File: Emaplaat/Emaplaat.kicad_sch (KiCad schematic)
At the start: 15 parts, among them IC1 ESP32-S3-WROOM-2-N32R16V, IC2 74HC595PW-Q100,118, IC3 74HC595PW-Q100,118

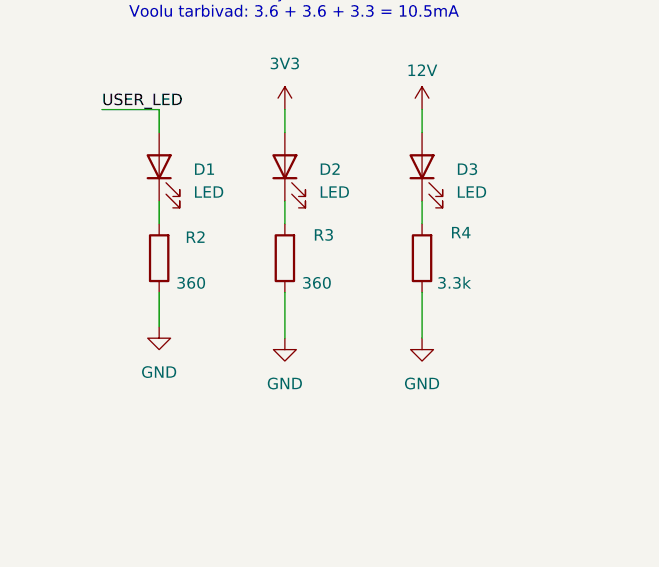
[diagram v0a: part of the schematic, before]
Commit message: ühe takisti muudatus
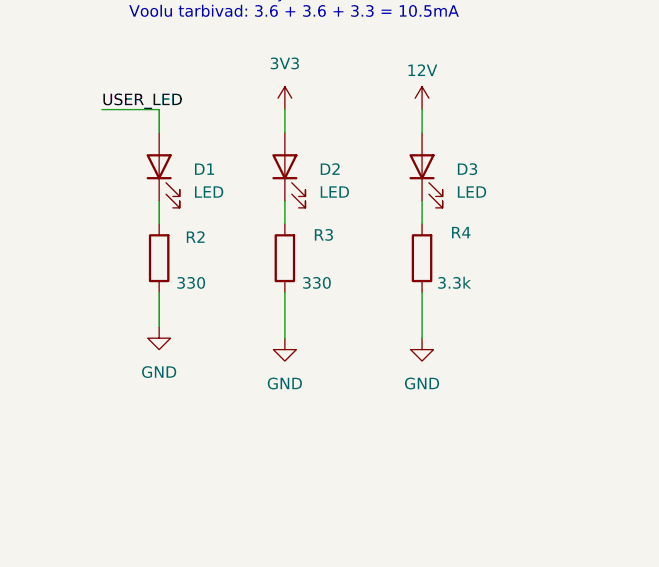
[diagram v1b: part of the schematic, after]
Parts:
- R2, R3: value 360 -> 330
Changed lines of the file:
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@@
 			)
 		)
-		(property "Value" "360"
+		(property "Value" "330"
 			(at 55.626 159.004 0)
 			(effects
@@
 			)
 		)
-		(property "Value" "360"
+		(property "Value" "330"
 			(at 41.656 159.004 0)
 			(effects

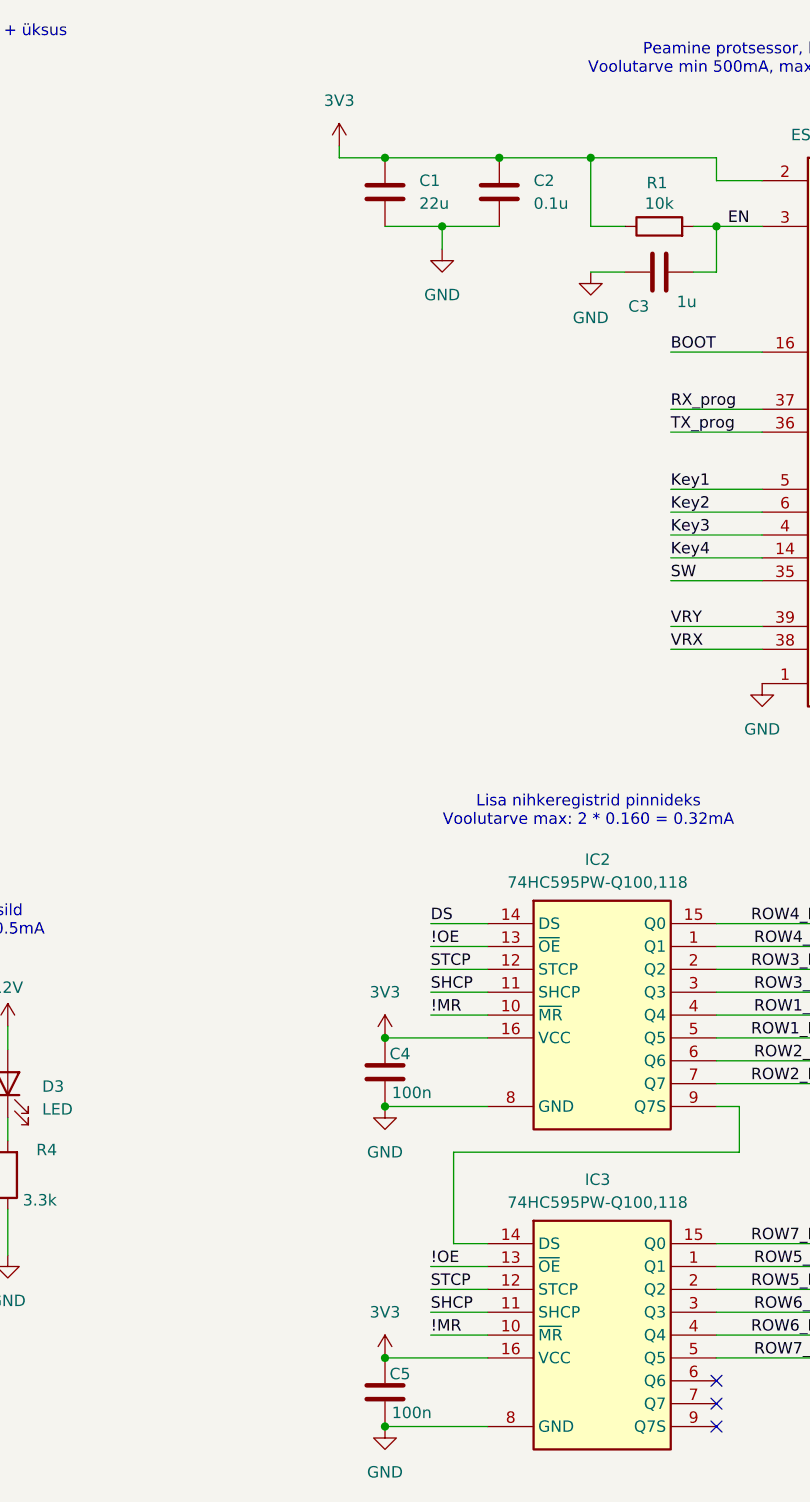
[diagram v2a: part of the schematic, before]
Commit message: Lisasin kondensaatorid, mis on >3.3u footprindi ja sümbolid. Sammuti liigutasin ESP32 ja USC-C ühendused plaadi äärtele
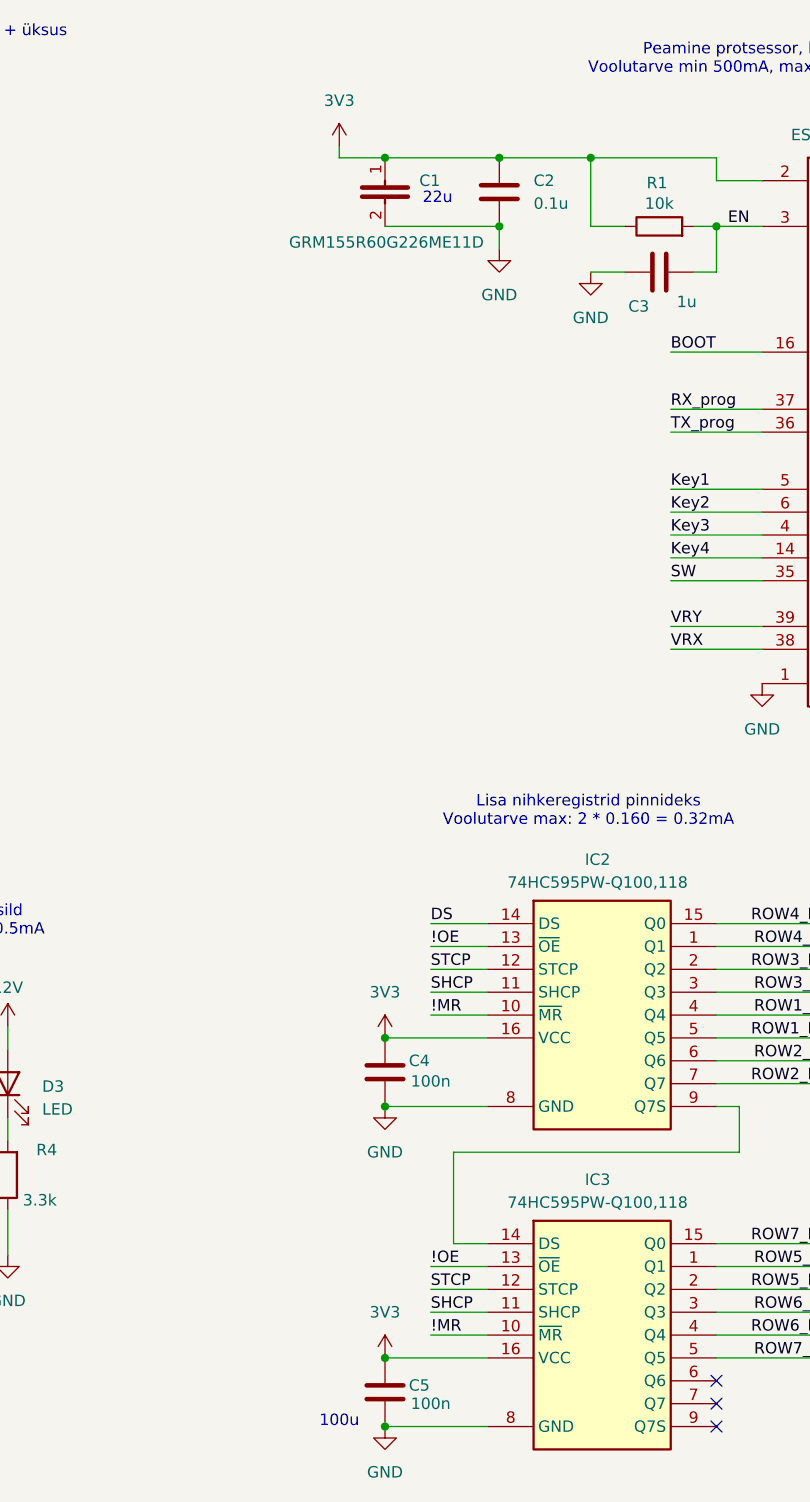
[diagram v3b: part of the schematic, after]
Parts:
- removed C1: 22u, Capacitor_SMD:C_0603_1608Metric_Pad1.08x0.95mm_HandSolder, symbol Device:C
- added C1: GRM155R60G226ME11D, CAPC1005X70N, symbol GRM155R60G226ME11D:GRM155R60G226ME11D
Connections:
- net 3V3: now also C4.2, C5.2, C1.1; no longer C4.1, C5.1
- net GND: now also C4.1, C5.1, C1.2; no longer C4.2, C5.2
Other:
- note added: "100u"
- note added: "22u"

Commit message: v1.2 bootstrapping pin parandus
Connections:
- net BOOT: now also IC1.27 (IO0); no longer IC1.16 (IO46)
- net COLUMN4: now also IC1.16 (IO46); no longer IC1.27 (IO0)
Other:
- note added: "IO0, IO3, IO45, IO46 on bootstrapping pinnid IO0 on vaja ainult kontollida bootmode'i jaoks"
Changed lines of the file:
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@@
+		)
+	)
+	(text "IO0, IO3, IO45, IO46 on bootstrapping pinnid\nIO0 on vaja ainult kontollida bootmode'i jaoks"
+		(exclude_from_sim no)
+		(at 116.332 67.31 0)
+		(effects
+			(font
+				(size 1.27 1.27)
+			)
 		)
 	)

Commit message: v1.3 pooleli
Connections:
- net !MR: now also IC1.12 (IO8); no longer IC1.13 (IO19)
- net !OE: now also IC1.11 (IO18); no longer IC1.10 (IO17)
- net COLUMN1: now also IC1.32 (IO39); no longer IC1.33 (IO40)
- net COLUMN10: now also IC1.19 (IO11); no longer IC1.21 (IO13)
- net COLUMN11: now also IC1.18 (IO10); no longer IC1.20 (IO12)
- net COLUMN12: now also IC1.17 (IO9); no longer IC1.19 (IO11)
- net COLUMN13: now also IC1.16 (IO46); no longer IC1.18 (IO10)
- net COLUMN14: now also IC1.15 (IO3); no longer IC1.17 (IO9)
- net COLUMN2: now also IC1.31 (IO38); no longer IC1.32 (IO39)
- net COLUMN3: now also IC1.26 (IO45); no longer IC1.31 (IO38)
- net COLUMN4: now also IC1.25 (IO48); no longer IC1.16 (IO46)
- net COLUMN5: now also IC1.24 (IO47); no longer IC1.26 (IO45)
- net COLUMN6: now also IC1.23 (IO21); no longer IC1.25 (IO48)
- net COLUMN7: now also IC1.22 (IO14); no longer IC1.24 (IO47)
- net COLUMN8: now also IC1.21 (IO13); no longer IC1.23 (IO21)
- net COLUMN9: now also IC1.20 (IO12); no longer IC1.22 (IO14)
- net DS: now also IC1.8 (IO15); no longer IC1.9 (IO16)
- net Key1: now also IC1.6 (IO6); no longer IC1.5 (IO5)
- net Key2: now also IC1.7 (IO7); no longer IC1.6 (IO6)
- net Key3: now also IC1.5 (IO5); no longer IC1.4 (IO4)
- net Key4: now also IC1.13 (IO19); no longer IC1.14 (IO20)
- net SHCP: now also IC1.9 (IO16); no longer IC1.12 (IO8)
- net STCP: now also IC1.10 (IO17); no longer IC1.11 (IO18)
- net USER_LED: now also IC1.14 (IO20); no longer IC1.15 (IO3)

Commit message: v1.4 peaagu
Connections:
- net !MR: now also IC1.9 (IO16); no longer IC1.12 (IO8)
- net !OE: now also IC1.12 (IO8); no longer IC1.11 (IO18)
- net ROW1_H: now also IC2.6 (Q6); no longer IC2.5 (Q5)
- net ROW1_L: now also IC2.7 (Q7); no longer IC2.4 (Q4)
- net ROW2_H: now also IC2.4 (Q4); no longer IC2.7 (Q7)
- net ROW2_L: now also IC2.5 (Q5); no longer IC2.6 (Q6)
- net ROW4_H: now also IC3.1 (Q1); no longer IC2.15 (Q0)
- net ROW5_H: now also IC3.3 (Q3); no longer IC3.2 (Q2)
- net ROW5_L: now also IC3.2 (Q2); no longer IC3.1 (Q1)
- net ROW6_H: now also IC3.5 (Q5); no longer IC3.4 (Q4)
- net ROW6_L: now also IC3.4 (Q4); no longer IC3.3 (Q3)
- net ROW7_H: now also IC3.7 (Q7); no longer IC3.15 (Q0)
- net ROW7_L: now also IC3.6 (Q6); no longer IC3.5 (Q5)
- net SHCP: now also IC1.10 (IO17); no longer IC1.9 (IO16)
- net STCP: now also IC1.11 (IO18); no longer IC1.10 (IO17)

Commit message: v1.5 valmis, juhendajad andsid rohelise tule
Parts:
- removed C1: GRM155R60G226ME11D, CAPC1005X70N, symbol GRM155R60G226ME11D:GRM155R60G226ME11D
- added C1: 22u, Capacitor_SMD:C_1206_3216Metric_Pad1.33x1.80mm_HandSolder, symbol Device:C
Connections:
- net 3V3: now also C1.1
- net GND: now also C1.2
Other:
- note removed: "22u"
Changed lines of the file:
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@@
-		)
-	)
-	(text "22u\n"
-		(exclude_from_sim no)
-		(at 115.062 47.752 0)
-		(effects
-			(font
-				(size 1.27 1.27)
-			)
 		)
 	)
@@
 	)
 	(junction
+		(at 109.22 43.18)
+		(diameter 0)
+		(color 0 0 0 0)
+	)
+	(junction
 		(at 109.22 140.97)
 		(diameter 0)
@@
 	)
 	(junction
-		(at 109.22 43.18)
-		(diameter 0)
-		(color 0 0 0 0)
-	)
-	(junction
 		(at 109.22 176.53)
 		(diameter 0)
@@
 	(wire
 		(pts
+			(xy 109.22 43.18) (xy 121.92 43.18)
+		)
+		(stroke
+			(width 0)
+			(type default)
+		)
+	)
+	(wire
+		(pts
 			(xy 109.22 176.53) (xy 120.65 176.53)
 		)
@@
 	(wire
 		(pts
-			(xy 109.22 43.18) (xy 121.92 43.18)
+			(xy 104.14 43.18) (xy 109.22 43.18)
 		)
 		(stroke
@@
 		(pts
 			(xy 232.41 87.63) (xy 246.38 87.63)
-		)
-		(stroke
-			(width 0)
-			(type default)
-		)
-	)
-	(wire
-		(pts
-			(xy 104.14 43.18) (xy 109.22 43.18)
 		)
 		(stroke
@@
 	)
 	(symbol
+		(lib_id "Device:C")
+		(at 109.22 46.99 0)
+		(unit 1)
+		(exclude_from_sim no)
+		(in_bom yes)
+		(on_board yes)
+		(dnp no)
+		(fields_autoplaced yes)
+		(property "Reference" "C1"
+			(at 113.03 45.7199 0)
+			(effects
+				(font
+					(size 1.27 1.27)
+				)
+				(justify left)
+			)
+		)
+		(property "Value" "22u"
+			(at 113.03 48.2599 0)
+			(effects
+				(font
+					(size 1.27 1.27)
+				)
+				(justify left)
+			)
+		)
+		(property "Footprint" "Capacitor_SMD:C_1206_3216Metric_Pad1.33x1.80mm_HandSolder"
+			(at 110.1852 50.8 0)
+			(effects
+				(font
+					(size 1.27 1.27)
+				)
+				(hide yes)
+			)
+		)
+		(property "Datasheet" "https://www.mouser.ee/ProductDetail/Samsung-Electro-Mechanics/CL31A226KAHNNNE?qs=sGAEpiMZZMsh%252B1woXyUXjxqcB7t9naYpIUTIw5YVtmc%3D"
+			(at 109.22 46.99 0)
+			(effects
+				(font
+					(size 1.27 1.27)
+				)
+				(hide yes)
+			)
+		)
+		(property "Description" "Unpolarized capacitor"
+			(at 109.22 46.99 0)
+			(effects
+				(font
+					(size 1.27 1.27)
+				)
+				(hide yes)
+			)
+		)
+		(pin "2"
+		)
+		(pin "1"
+		)
+		(instances
+			(project "Emaplaat"
+				(path "/489224c0-ace1-4530-aa61-a5d03adf1434"
+					(reference "C1")
+					(unit 1)
+				)
+			)
+		)
+	)
+	(symbol
 		(lib_id "power:GND")
 		(at 109.22 148.59 0)
@@
 					(unit 1)
 				)
-			)
-		)
-	)
-	(symbol
-		(lib_id "GRM155R60G226ME11D:GRM155R60G226ME11D")
-		(at 109.22 40.64 270)
-		(unit 1)
-		(exclude_from_sim no)
-		(in_bom yes)
-		(on_board yes)
-		(dnp no)
-		(property "Reference" "C1"
-			(at 113.03 45.7199 90)
-			(effects
-				(font
-					(size 1.27 1.27)
-				)
-				(justify left)
-			)
-		)
-		(property "Value" "GRM155R60G226ME11D"
-			(at 98.552 52.578 90)
-			(effects
-				(font
-					(size 1.27 1.27)
-				)
-				(justify left)
-			)
-		)
-		(property "Footprint" "CAPC1005X70N"
-			(at 13.03 49.53 0)
-			(effects
-				(font
-					(size 1.27 1.27)
-				)
-				(justify left top)
-				(hide yes)
-			)
-		)
-		(property "Datasheet" "http://www.murata.com/~/media/webrenewal/support/library/catalog/products/capacitor/mlcc/c02e.pdf"
-			(at -86.97 49.53 0)
-			(effects
-				(font
-					(size 1.27 1.27)
-				)
-				(justify left top)
-				(hide yes)
-			)
-		)
-		(property "Description" "Chip Capacitor value 226"
-			(at 125.476 45.212 0)
-			(effects
-				(font
-					(size 1.27 1.27)
-				)
-				(hide yes)
-			)
-		)
-		(property "Height" "0.7"
-			(at -286.97 49.53 0)
-			(effects
-				(font
-					(size 1.27 1.27)
-				)
-				(justify left top)
-				(hide yes)
-			)
-		)
-		(property "Mouser Part Number" "81-GRM155R60G226ME1D"
-			(at -386.97 49.53 0)
-			(effects
-				(font
-					(size 1.27 1.27)
-				)
-				(justify left top)
-				(hide yes)
-			)
-		)
-		(property "Mouser Price/Stock" "https://www.mouser.co.uk/ProductDetail/Murata-Electronics/GRM155R60G226ME11D?qs=9Bj94LTQhPD05IUpc3I6Ow%3D%3D"
-			(at -486.97 49.53 0)
-			(effects
-				(font
-					(size 1.27 1.27)
-				)
-				(justify left top)
-				(hide yes)
-			)
-		)
-		(property "Manufacturer_Name" "Murata Electronics"
-			(at -586.97 49.53 0)
-			(effects
-				(font
-					(size 1.27 1.27)
-				)
-				(justify left top)
-				(hide yes)
-			)
-		)
-		(property "Manufacturer_Part_Number" "GRM155R60G226ME11D"
-			(at -686.97 49.53 0)
-			(effects
-				(font
-					(size 1.27 1.27)
-				)
-				(justify left top)
-				(hide yes)
-			)
-		)
-		(pin "2"
-		)
-		(pin "1"
-		)
-		(instances
-			(project "Emaplaat"
-				(path "/489224c0-ace1-4530-aa61-a5d03adf1434"
-					(reference "C1")
-					(unit 1)
-				)
